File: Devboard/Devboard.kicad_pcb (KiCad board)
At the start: 2 copper layers, 64.4 x 35.5 mm, 36 parts, among them IC1 114993390, J1 USB_C_Receptacle_USB2.0_16P, J2 SWD, J3 RMF, SW1 SHPHLD, SW2 RST, SW3 SW_Push, U1 NPM1304-QEAA-R, U2 E73-2G4M08S1C, U3 SRV05-4, Y1 32.768

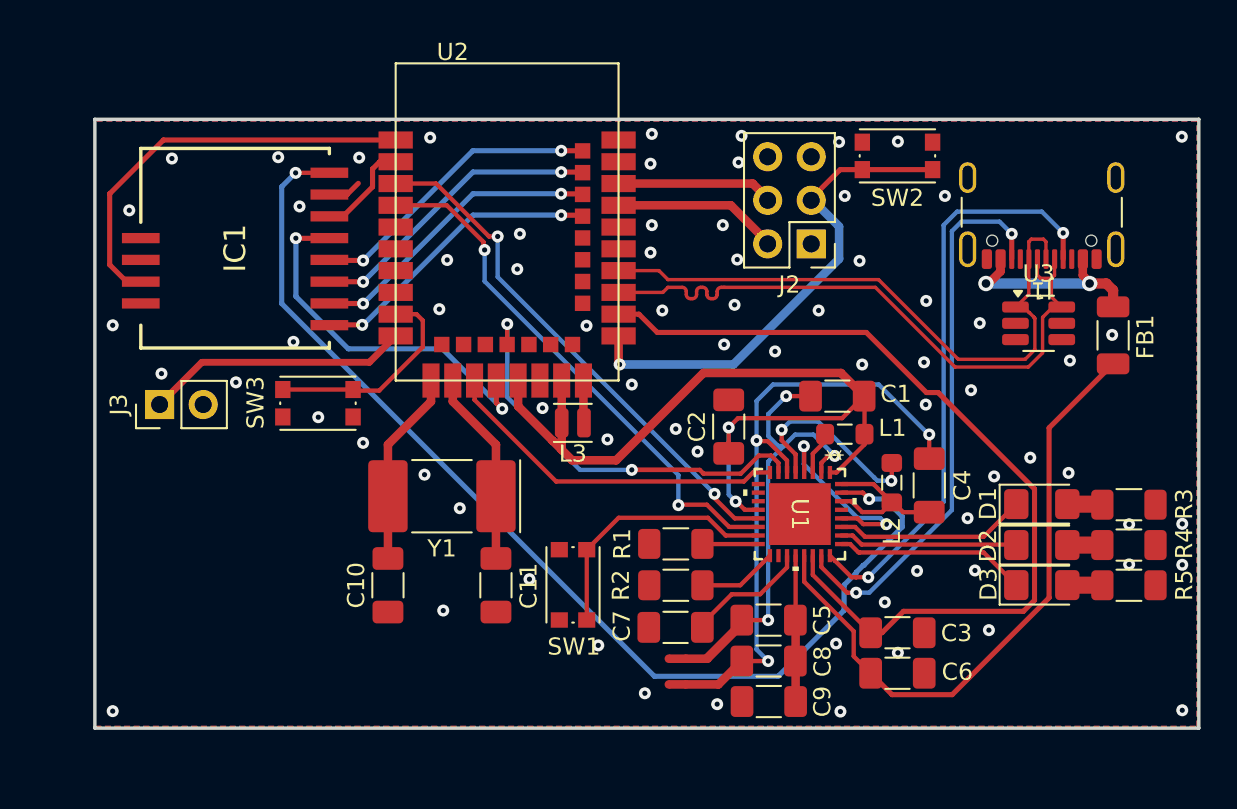
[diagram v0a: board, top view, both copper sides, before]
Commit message: added sd card, and refined design
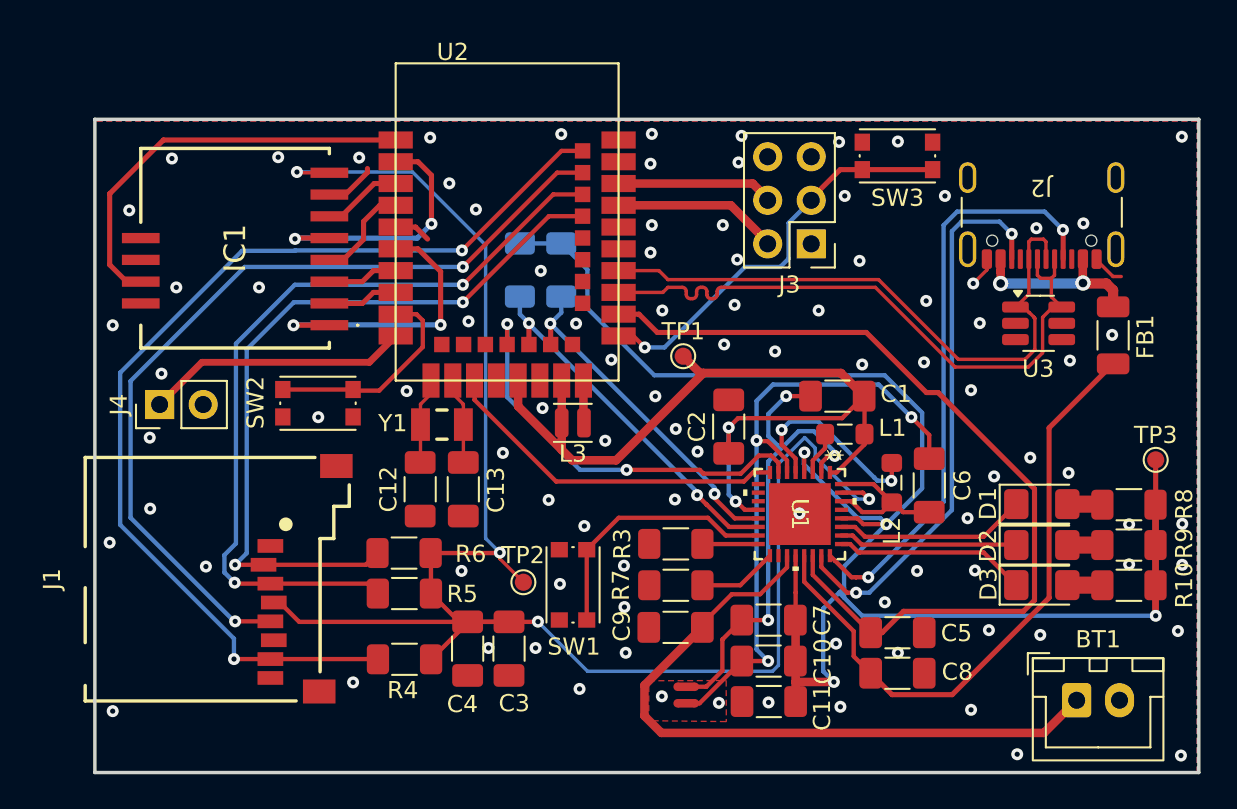
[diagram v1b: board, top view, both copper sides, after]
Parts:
- added BT1: 1S Lipo, Connector_JST:JST_XH_B2B-XH-A_1x02_P2.50mm_Vertical, F.Cu at (195.7, 71.4)
- added C3: 0.1u, Capacitor_SMD:C_1206_3216Metric_Pad1.33x1.80mm_HandSolder, F.Cu at (162.6, 68.4)
- added C4: 10u, Capacitor_SMD:C_1206_3216Metric_Pad1.33x1.80mm_HandSolder, F.Cu at (160.1, 68.4)
- added J1: 693071010811, 693071010811:693071010811, F.Cu at (145.5, 64.3)
- added R1: 4k7, Resistor_SMD:R_1206_3216Metric_Pad1.30x1.75mm_HandSolder, B.Cu at (165.6, 46.3)
- added R2: 4k7, Resistor_SMD:R_1206_3216Metric_Pad1.30x1.75mm_HandSolder, B.Cu at (163.2, 46.3)
- added R4: 47k, Resistor_SMD:R_1206_3216Metric_Pad1.30x1.75mm_HandSolder, F.Cu at (156.5, 69.0)
- added R5: 47k, Resistor_SMD:R_1206_3216Metric_Pad1.30x1.75mm_HandSolder, F.Cu at (156.5, 65.2)
- added R6: 47k, Resistor_SMD:R_1206_3216Metric_Pad1.30x1.75mm_HandSolder, F.Cu at (156.4, 62.8)
- added TP1: VMCU, TestPoint:TestPoint_Pad_D1.0mm, F.Cu at (172.7, 51.3)
- added TP2: 3V3, TestPoint:TestPoint_Pad_D1.0mm, F.Cu at (163.4, 64.5)
- added TP3: VSYS, TestPoint:TestPoint_Pad_D1.0mm, F.Cu at (200.3, 57.4)
- C2: value 100n -> 0.1u
- Y1: footprint Crystal:Crystal_SMD_MicroCrystal_CC1V-T1A-2Pin_8.0x3.7mm -> Project_Components:WE-XTAL_CFPX-217
- moved C13 5.92 mm to (159.9, 59.1)
- moved C12 5.91 mm to (157.4, 59.1)
- moved Y1 4.18 mm to (158.6, 55.3)
- moved NT1 1.71 mm to (172.9, 70.6)
- moved NT2 1.21 mm to (172.9, 71.6)
- renumbered C8 to C10, C9 to C11, C10 to C12, C11 to C13, C3 to C5, C4 to C6, C5 to C7, C6 to C8, C7 to C9, J1 to J2, J2 to J3, J3 to J4, R5 to R10, R1 to R3, R2 to R7, R3 to R8, R4 to R9, SW3 to SW2, SW2 to SW3
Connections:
- J2 pad SH: GND -> (no net)
- U2 pad 17: LoRa_RST -> unconnected-(U2C-P1.09-Pad17)
- U2 pad 2: LoRa_NSS -> LoRa_RST
- U2 pad 20: unconnected-(U2B-P0.12-Pad20) -> SCL
- U2 pad 22: unconnected-(U2B-P0.07-Pad22) -> SDA
- U2 pad 3: SDA -> LoRa_NSS
- U2 pad 36: LoRa_SW -> CS
- U2 pad 38: LoRa_MISO -> MOSI
- U2 pad 4: SCL -> LoRa_SCK
- U2 pad 40: LoRa_MOSI -> SCK
- U2 pad 42: LoRa_SCK -> MISO
- U2 pad 6: unconnected-(U2C-P1.13-Pad6) -> LoRa_SW
- U2 pad 7: unconnected-(U2B-P0.02/AIN0-Pad7) -> LoRa_MOSI
- U2 pad 8: unconnected-(U2B-P0.29/AIN5-Pad8) -> LoRa_MISO
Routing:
- net VSYS: track 20.2 -> 97.6 mm, vias 2 -> 4
- net MISO: track 0.00 -> 60.2 mm, vias 0 -> 2
- net SCK: track 0.00 -> 50.1 mm, vias 0 -> 2
- net MOSI: track 0.00 -> 46.9 mm, vias 0 -> 2
- net CS: track 0.00 -> 44.3 mm, vias 0 -> 2
- net +3.3V: track 64.4 -> 102.4 mm, vias 2 -> 4
- net VBAT: track 7.20 -> 40.2 mm
- net LoRa_MISO: track 17.4 -> 4.13 mm, vias 2 -> 0
- net LoRa_MOSI: track 17.4 -> 4.13 mm, vias 2 -> 0
- net LoRa_SCK: track 17.4 -> 5.80 mm, vias 2 -> 0
- net SDA: track 30.8 -> 20.3 mm
- net SCL: track 31.2 -> 21.5 mm
- net GND: track 1.96 -> 8.78 mm, vias 73 -> 94
- net Net-(U2B-P0.01/XL2): track 11.4 -> 5.04 mm
- net Net-(U2B-P0.00/XL1): track 11.4 -> 5.04 mm
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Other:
- board size 64.4 x 35.5 mm -> 64.4 x 38.1 mm

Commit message: Added external pin
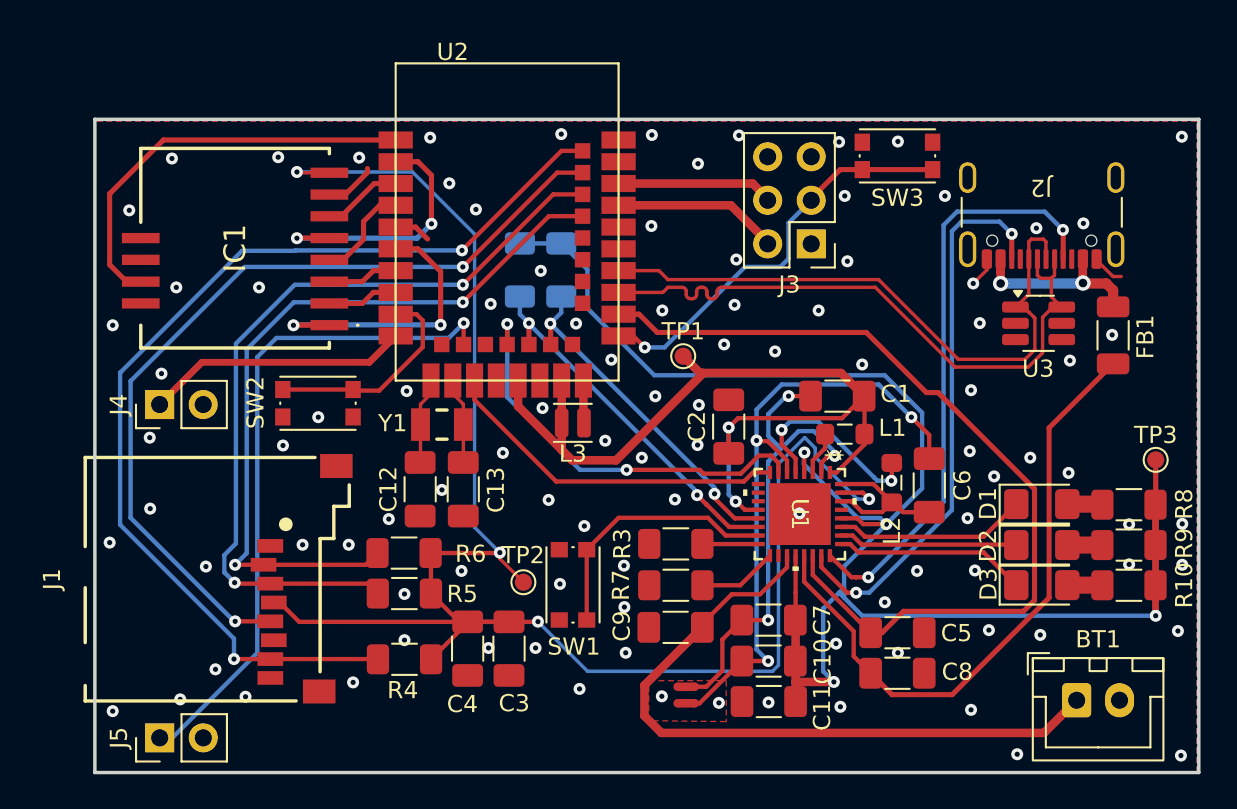
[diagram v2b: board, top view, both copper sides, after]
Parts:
- added J5: RMF, Connector_PinHeader_2.54mm:PinHeader_1x02_P2.54mm_Vertical, F.Cu at (142.2, 73.6)
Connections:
- J2 pad SH: (no net) -> GND
- U2 pad 14: unconnected-(U2B-P0.06-Pad14) -> EXT_PIN
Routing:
- net EXT_PIN: track 0.00 -> 39.1 mm, vias 0 -> 1
- net GND: vias 94 -> 101

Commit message: Added 3V3 output
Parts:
- J5: value RMF -> EXT_PIN; footprint Connector_PinHeader_2.54mm:PinHeader_1x02_P2.54mm_Vertical -> Connector_PinHeader_2.54mm:PinHeader_1x03_P2.54mm_Vertical
- moved J5 0.08 mm to (142.1, 73.5)
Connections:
- J2 pad SH: GND -> (no net)
- J5 pad 2: GND -> +3V3

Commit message: Final commit
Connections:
- J2 pad SH: (no net) -> GND
- J3 pad 1: +3V3 -> +3.3V
- J5 pad 2: +3V3 -> +3.3V
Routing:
- net +3.3V: track 102.4 -> 163.0 mm, vias 4 -> 5
- net GND: vias 101 -> 102
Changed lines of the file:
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@@
 			(layers "*.Cu" "*.Mask" "F.Paste")
 			(remove_unused_layers no)
+			(net "GND")
 		)
 		(pad "SH" thru_hole oval
@@
 			(layers "*.Cu" "*.Mask" "F.Paste")
 			(remove_unused_layers no)
+			(net "GND")
 		)
 		(pad "SH" thru_hole oval
@@
 			(layers "*.Cu" "*.Mask" "F.Paste")
 			(remove_unused_layers no)
+			(net "GND")
 		)
 		(pad "SH" thru_hole oval
@@
 			(layers "*.Cu" "*.Mask" "F.Paste")
 			(remove_unused_layers no)
+			(net "GND")
 		)
 		(embedded_fonts no)
@@
 			(layers "*.Cu" "*.Mask")
 			(remove_unused_layers no)
-			(net "+3V3")
+			(net "+3.3V")
 			(pinfunction "Pin_1_1")
 			(pintype "passive")
@@
 			(net "unconnected-(J1-VSS-Pad6)")
 			(pinfunction "VSS_6")
-			(pintype "bidirectional")
+			(pintype "bidirectional+no_connect")
 			(solder_mask_margin 0.102)
 		)
@@
 			(net "unconnected-(U2C-P1.09-Pad17)")
 			(pinfunction "P1.09_17")
-			(pintype "bidirectional")
+			(pintype "bidirectional+no_connect")
 			(solder_mask_margin 0.102)
 		)
@@
 			(layers "*.Cu" "*.Mask")
 			(remove_unused_layers no)
-			(net "+3V3")
+			(net "+3.3V")
 			(pinfunction "Pin_2_2")
 			(pintype "passive")
@@
 	)
 	(via
+		(at 193.675 38.8366)
+		(size 0.7)
+		(drill 0.3)
+		(layers "F.Cu" "B.Cu")
+		(free yes)
+		(net "GND")
+	)
+	(via
 		(at 155.5496 60.8076)
 		(size 0.7)
@@
 	)
 	(via
+		(at 150.2918 66.8528)
+		(size 0.7)
+		(drill 0.3)
+		(layers "F.Cu" "B.Cu")
+		(net "+3.3V")
+	)
+	(via
 		(at 162.0266 62.7634)
 		(size 0.7)
@@
 	)
 	(segment
+		(start 163.651271 41.0878)
+		(end 160.5534 44.185671)
+		(width 0.2)
+		(layer "B.Cu")
+		(net "+3.3V")
+	)
+	(segment
 		(start 177.92413 69.688)
 		(end 178.275601 69.336529)
@@
 	)
 	(segment
+		(start 150.2918 66.8528)
+		(end 150.3426 66.802)
+		(width 0.2)
+		(layer "B.Cu")
+		(net "+3.3V")
+	)
+	(segment
+		(start 163.658071 41.081)
+		(end 160.5534 44.185671)
+		(width 0.15)
+		(layer "B.Cu")
+		(net "+3.3V")
+	)
+	(segment
 		(start 178.275601 69.336529)
 		(end 178.275601 57.587556)
@@
 	)
 	(segment
+		(start 180.1876 44.7548)
+		(end 181.3146 43.6278)
+		(width 0.2)
+		(layer "B.Cu")
+		(net "+3.3V")
+	)
+	(segment
 		(start 179.809357 56.0538)
 		(end 180.419183 56.663626)
@@
 	)
 	(segment
+		(start 181.3146 43.6278)
+		(end 181.3146 41.747981)
+		(width 0.2)
+		(layer "B.Cu")
+		(net "+3.3V")
+	)
+	(segment
+		(start 144.6784 72.4662)
+		(end 150.2918 66.8528)
+		(width 0.2)
+		(layer "B.Cu")
+		(net "+3.3V")
+	)
+	(segment
+		(start 144.6784 73.5076)
+		(end 144.6784 72.4662)
+		(width 0.2)
+		(layer "B.Cu")
+		(net "+3.3V")
+	)
+	(segment
 		(start 180.419183 57.178383)
 		(end 182.88 59.6392)
@@
 	)
 	(segment
+		(start 180.1876 44.7548)
+		(end 181.2626 43.6798)
+		(width 0.15)
+		(layer "B.Cu")
+		(net "+3.3V")
+	)
+	(segment
 		(start 162.0266 62.7634)
 		(end 160.5534 61.2902)
@@
 	)
 	(segment
+		(start 181.3146 41.747981)
+		(end 180.654419 41.0878)
+		(width 0.2)
+		(layer "B.Cu")
+		(net "+3.3V")
+	)
+	(segment
 		(start 167.1478 69.688)
 		(end 177.92413 69.688)
@@
 	)
 	(segment
+		(start 180.57408 41.081)
+		(end 163.658071 41.081)
+		(width 0.15)
+		(layer "B.Cu")
+		(net "+3.3V")
+	)
+	(segment
+		(start 180.654419 41.0878)
+		(end 163.651271 41.0878)
+		(width 0.2)
+		(layer "B.Cu")
+		(net "+3.3V")
+	)
+	(segment
 		(start 164.2491 66.7893)
 		(end 167.1478 69.688)
@@
 	)
 	(segment
+		(start 181.2626 43.6798)
+		(end 181.2626 41.76952)
+		(width 0.15)
+		(layer "B.Cu")
+		(net "+3.3V")
+	)
+	(segment
 		(start 160.5534 61.2902)
 		(end 160.5534 44.185671)
@@
 	)
 	(segment
+		(start 181.2626 41.76952)
+		(end 180.57408 41.081)
+		(width 0.15)
+		(layer "B.Cu")
+		(net "+3.3V")
+	)
+	(segment
 		(start 180.419183 56.663626)
 		(end 180.419183 57.178383)
@@
 			)
 		)
+	)
+	(zone
+		(layer "B.Cu")
+		(hatch edge 0.5)
+		(connect_pads
+			(clearance 0)
+		)
+		(min_thickness 0.25)
+		(keepout
+			(tracks allowed)
+			(vias allowed)
+			(pads allowed)
+			(copperpour not_allowed)
+			(footprints allowed)
+		)
+		(placement
+			(enabled no)
+			(sheetname "/")
+		)
+		(fill
+			(thermal_gap 0.5)
+			(thermal_bridge_width 0.5)
+			(island_removal_mode 0)
+		)
+		(polygon
+			(pts
+				(xy 149.538821 67.6656) (xy 147.877689 67.6656) (xy 147.877689 66.0146) (xy 150.263291 66.0146)
+			)
+		)
